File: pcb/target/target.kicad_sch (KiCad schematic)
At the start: 11 parts, among them J1 Pogo_01x06_female, J2 Pogo_01x06_male, Q1 SI2333CDS-HXY

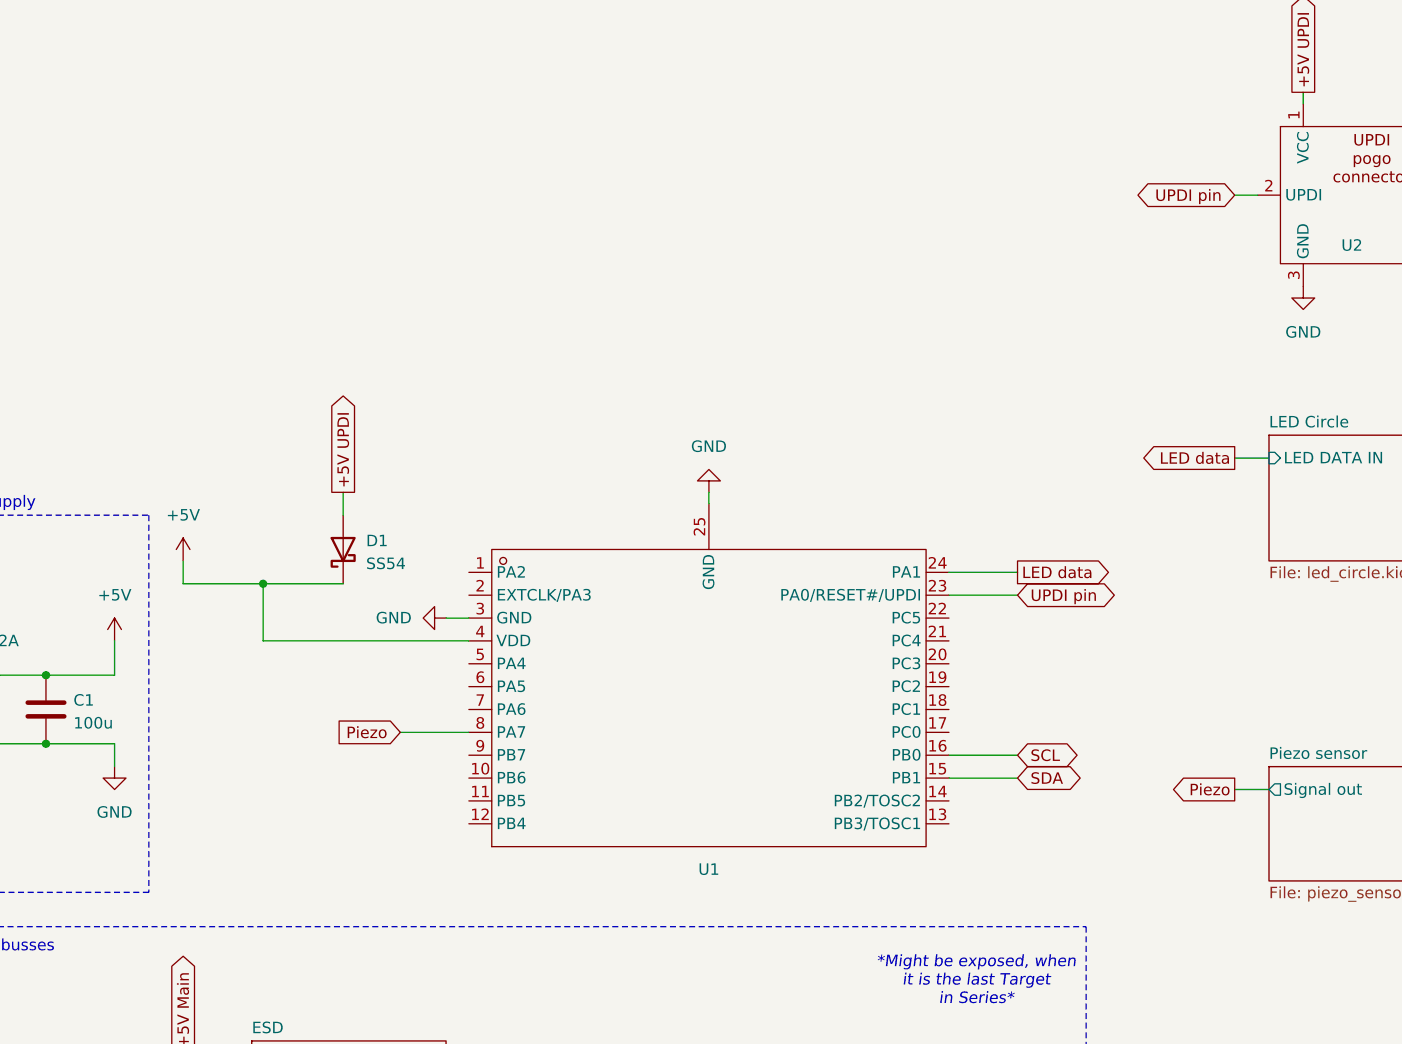
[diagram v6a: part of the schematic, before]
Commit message: Switched to attiny1614 and fixed esd for the i2c lines (target pcb)
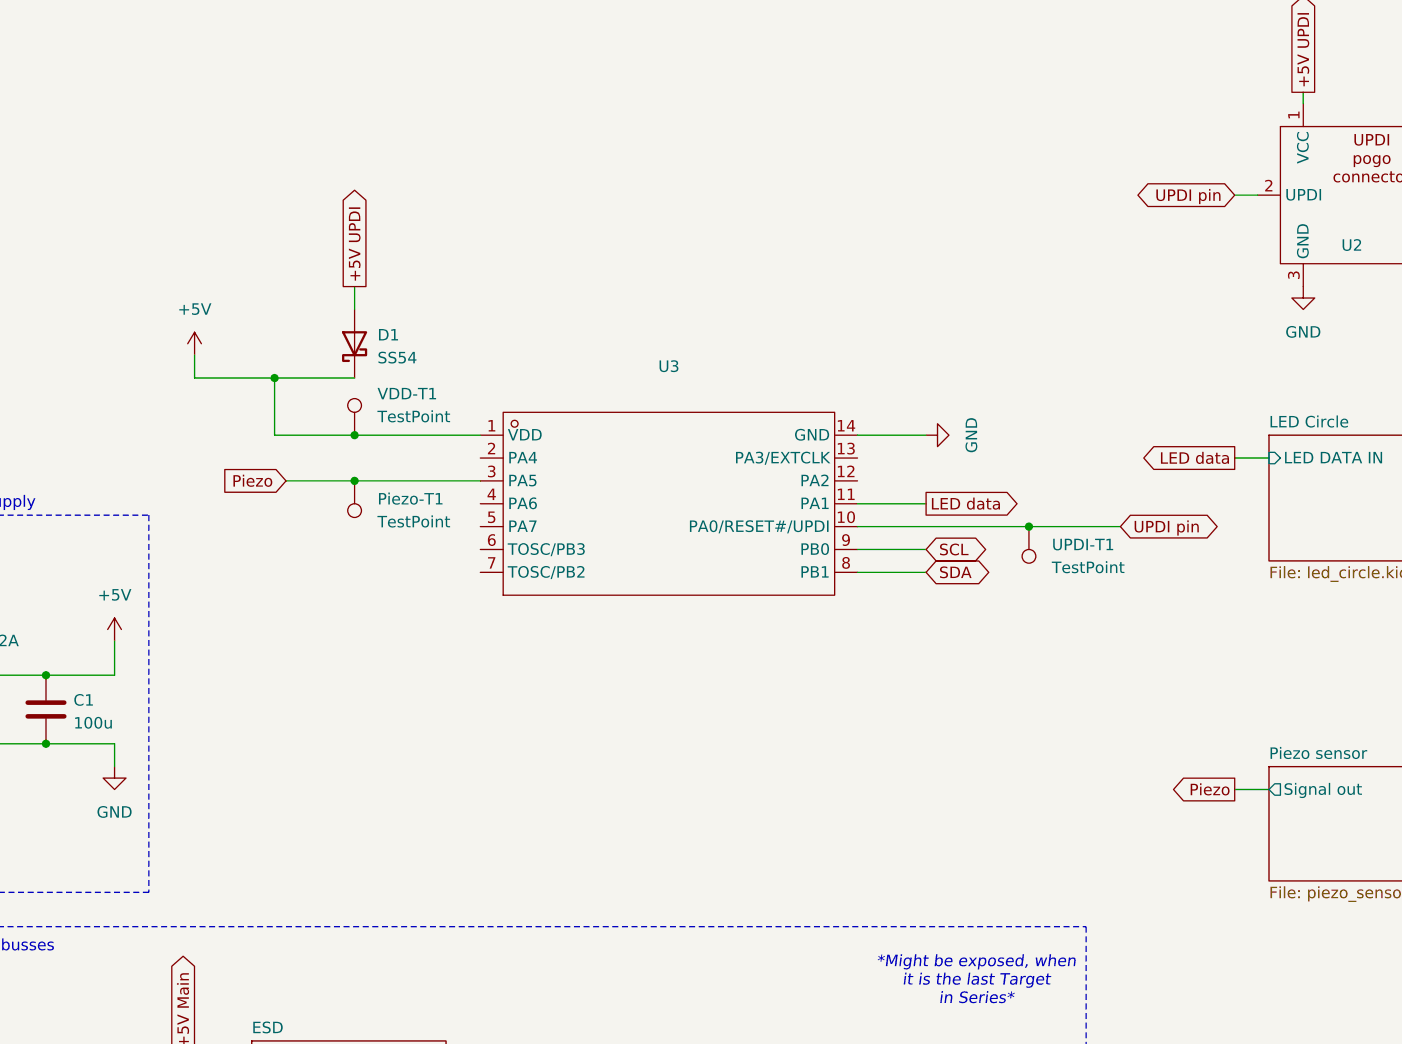
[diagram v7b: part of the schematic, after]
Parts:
- removed U1: ~, custom_footprints:WQFN-24_L4.0-W4.0-P0.50-TL-EP2.6, symbol custom_symbols:ATTINY3217-MFR
- added Piezo-T1, UPDI-T1, VDD-T1: TestPoint, TestPoint:TestPoint_Pad_D1.5mm, symbol Connector:TestPoint
- added U3: ~, custom_footprints:SOIC-14_L8.7-W3.9-P1.27-LS6.0-BL, symbol custom_symbols:ATTINY1614-SSF
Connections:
- net +5V: now also U3.1 (VDD), VDD-T1.1
- net GND: now also U3.14 (GND)
- net LED data: now also U3.11 (PA1)
- net Piezo: now also Piezo-T1.1, U3.3 (PA5)
- net SCL: now also U3.9 (PB0)
- net SDA: now also U3.8 (PB1)
- net UPDI pin: now also U3.10 (PA0/RESET#/UPDI), UPDI-T1.1
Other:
- moved on the sheet: D1

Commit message: Initial commit for v2
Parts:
- removed C1: 100u, Capacitor_SMD:C_1206_3216Metric, symbol Device:C
- removed D1: SS54, Diode_SMD:D_SMA, symbol Device:D_Schottky
- removed F1: Polyfuse IT2A, Fuse:Fuse_2920_7451Metric, symbol Device:Polyfuse
- removed J1: Pogo_01x06_female, custom_footprints:01x06 SMD 4x4mm pad, symbol custom_symbols:Pogo_01x06_female
- removed J2: Pogo_01x06_male, custom_footprints:01x06 SMD 4x4mm pad, symbol custom_symbols:Pogo_01x06_male
- removed JP2: SolderJumper_2_Open, Jumper:SolderJumper-2_P1.3mm_Open_TrianglePad1.0x1.5mm, symbol Jumper:SolderJumper_2_Open
- removed Piezo-T1, UPDI-T1, VDD-T1: TestPoint, TestPoint:TestPoint_Pad_D1.5mm, symbol Connector:TestPoint
- removed Q1: SI2333CDS-HXY, custom_footprints:SOT23, symbol SI2333CD:SI2333CDS-T1-GE3
- removed R1: 47kR, Resistor_SMD:R_0805_2012Metric, symbol Device:R
- removed R2: 10kR, Resistor_SMD:R_0805_2012Metric, symbol Device:R
- removed U2: ~, updi_pogo:P2,54_MH3_pogo_updi, symbol updi_pogo:updi_pogo_connector
- removed U3: ~, custom_footprints:SOIC-14_L8.7-W3.9-P1.27-LS6.0-BL, symbol custom_symbols:ATTINY1614-SSF
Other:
- removed sheet ESD
- removed sheet LED Circle
- removed sheet Piezo sensor
- note removed: "*Might be exposed, when it is the last Target in Series*"
- note removed: "Main supply and data busses"
- note removed: "Main supply to local supply"
- note removed: "Restrict current when UPDI VCC present"
